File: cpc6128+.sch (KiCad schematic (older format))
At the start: 0 parts

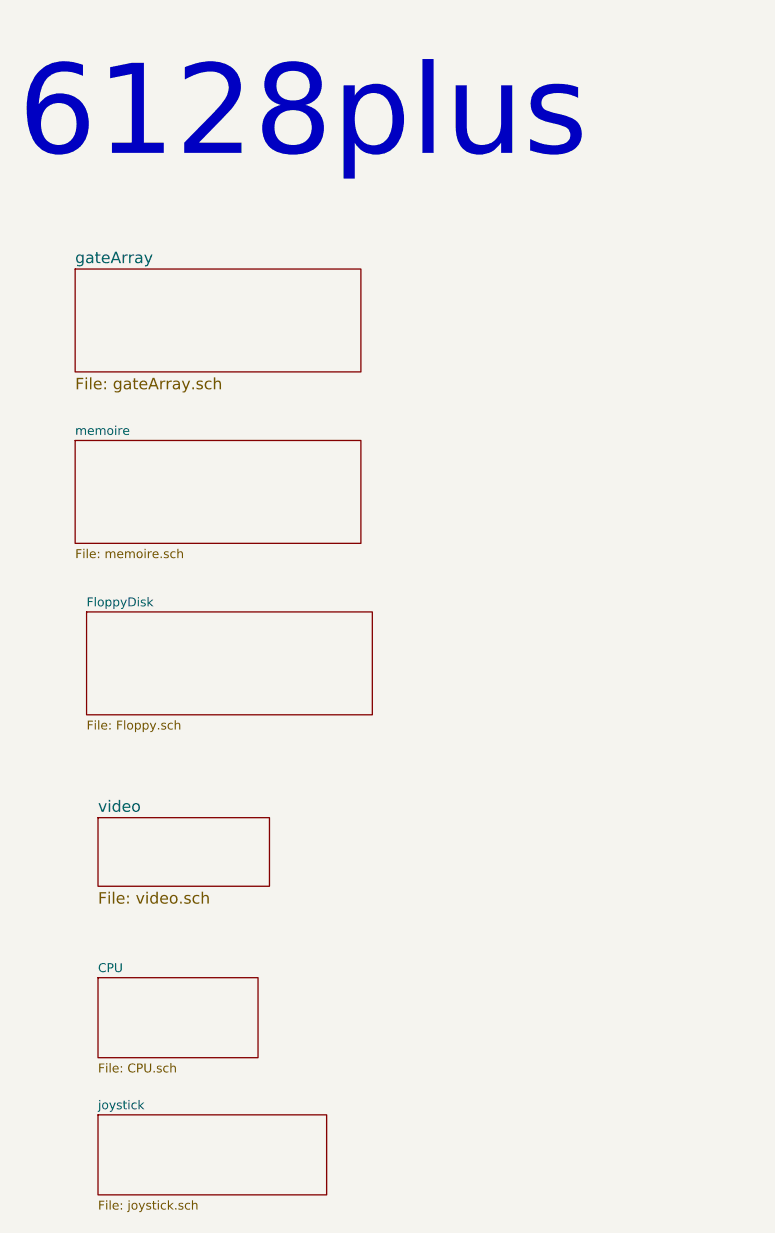
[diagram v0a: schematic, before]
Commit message: 29-03-2021 : first usage of hierarchical labels. focus on CPU/ Cartridge Connector
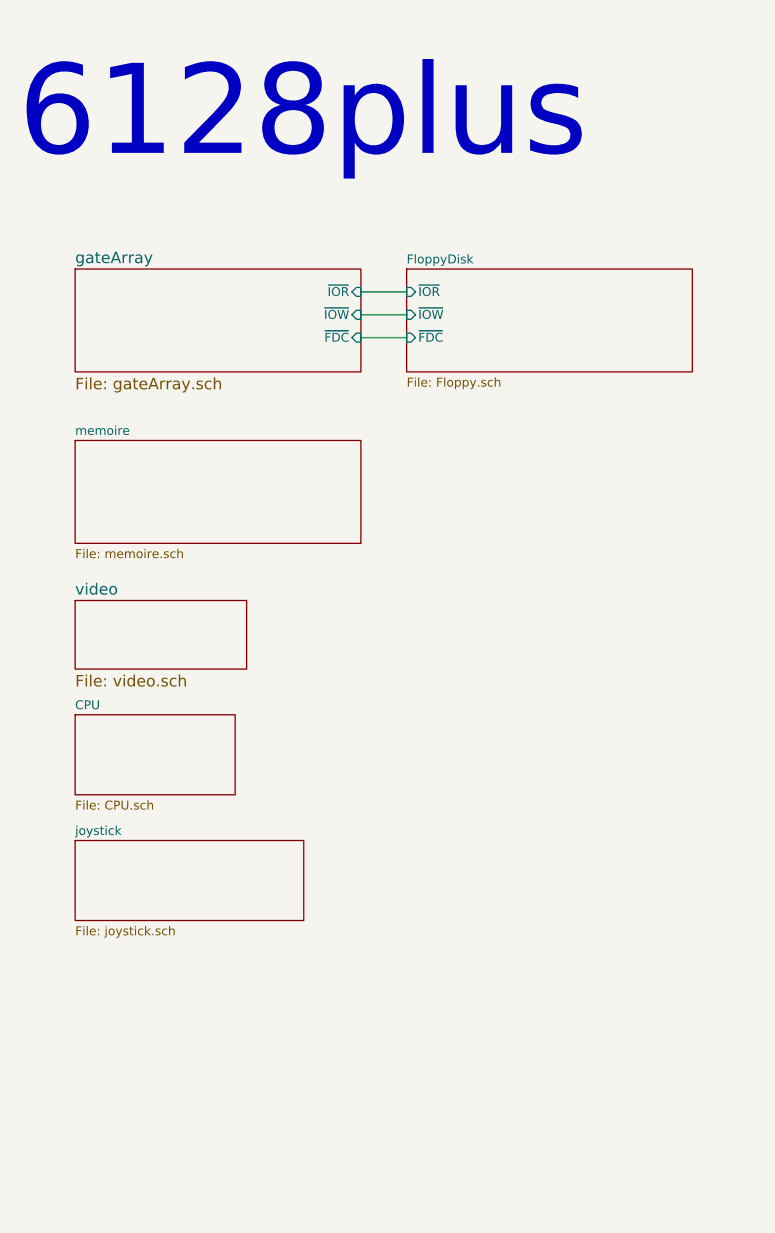
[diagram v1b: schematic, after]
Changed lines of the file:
@@
 F0 "gateArray" 50
 F1 "gateArray.sch" 50
+F2 "~IOR" I R 2450 1850 39
+F3 "~IOW" I R 2450 1950 39
+F4 "~FDC" I R 2450 2050 39
 $EndSheet
 $Sheet
-S 1300 4150 750  300
+S 1200 3200 750  300
 U 60517D0A
 F0 "video" 50
@@
 $EndSheet
 $Sheet
-S 1300 4850 700  350
+S 1200 3700 700  350
 U 607E3316
 F0 "CPU" 39
@@
 $EndSheet
 $Sheet
-S 1250 3250 1250 450
+S 2650 1750 1250 450
 U 6259ACB2
 F0 "FloppyDisk" 39
 F1 "Floppy.sch" 39
+F2 "~IOR" I L 2650 1850 39
+F3 "~IOW" I L 2650 1950 39
+F4 "~FDC" I L 2650 2050 39
 $EndSheet
 $Sheet
-S 1300 5450 1000 350
+S 1200 4250 1000 350
 U 631EEA59
 F0 "joystick" 39
@@
 Text Notes 950  1300 0    394  ~ 0
 6128plus\n
+Wire Wire Line
+	2450 1850 2650 1850
+Wire Wire Line
+	2450 1950 2650 1950
+Wire Wire Line
+	2450 2050 2650 2050
 $EndSCHEMATC
